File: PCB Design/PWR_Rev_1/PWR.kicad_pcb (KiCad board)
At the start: 2 copper layers, 40 x 65 mm, 57 parts, among them J1 Conn_01x24_Pin, J2 Conn_01x24_Pin, U1 LMR33630ADDA, U2 LMR33630ADDA, U3 LMR33630ADDA

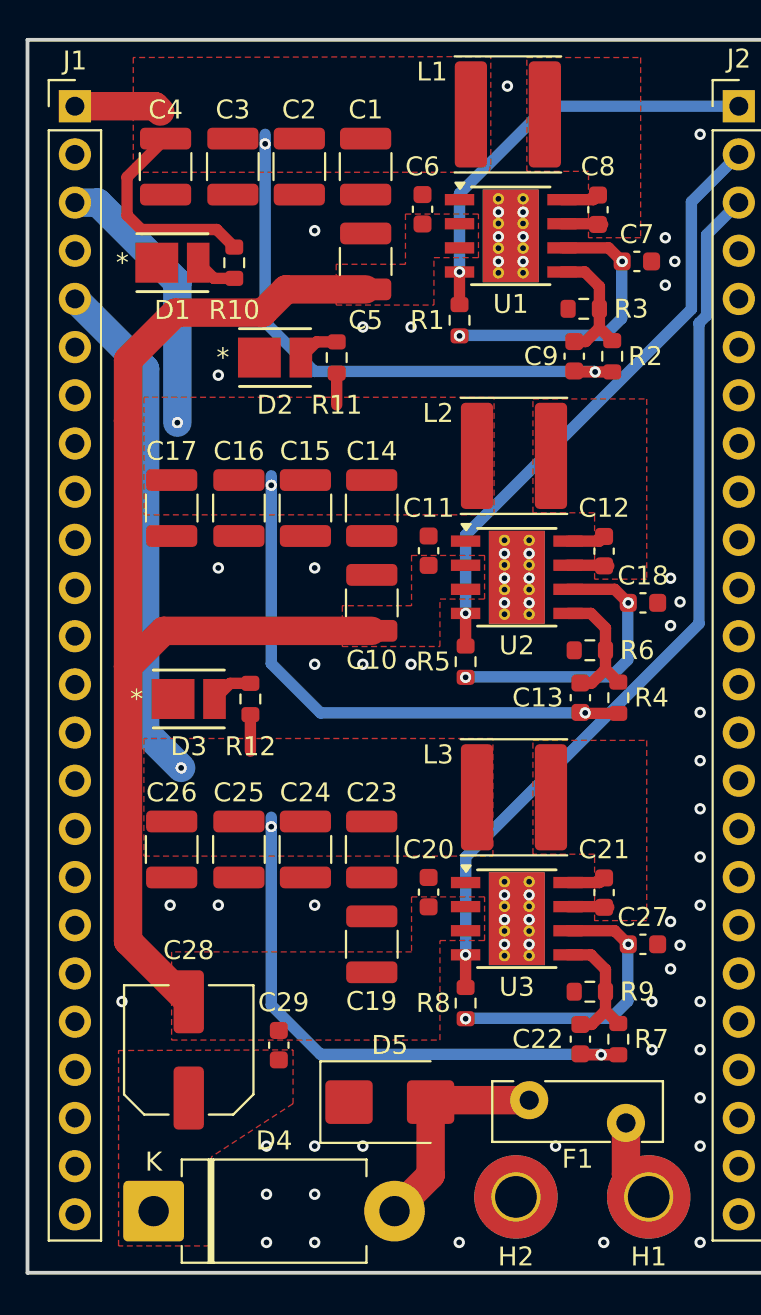
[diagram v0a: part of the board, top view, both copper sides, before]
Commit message: Fixed Schematic Errors
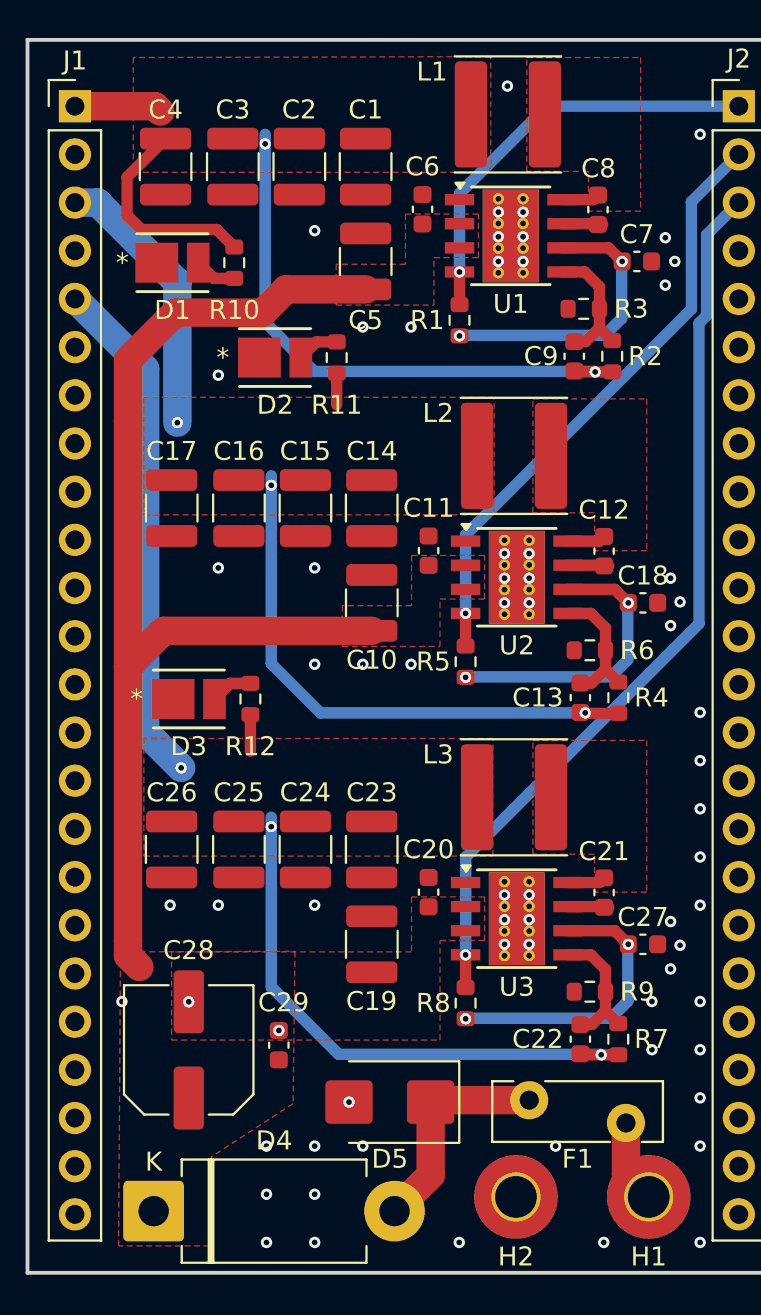
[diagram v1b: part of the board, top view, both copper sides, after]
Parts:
- R7: value 100k -> N/A
- R9: value 9.09k -> N/A
- turned C12 to -90 degrees
- turned C21 to -90 degrees
- turned C8 to -90 degrees
- turned D5 to 180 degrees
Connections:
- C12 pad 1: Net-(U2-BOOT) -> Net-(U2-SW)
- C12 pad 2: Net-(U2-SW) -> Net-(U2-BOOT)
- C21 pad 1: Net-(U3-BOOT) -> Net-(U3-SW)
- C21 pad 2: Net-(U3-SW) -> Net-(U3-BOOT)
- C28 pad 1: Net-(D4-K) -> VIN
- C28 pad 2: VIN -> GND
- C29 pad 1: Net-(D4-K) -> VIN
- C29 pad 2: VIN -> GND
- C8 pad 1: Net-(U1-BOOT) -> Net-(U1-SW)
- C8 pad 2: Net-(U1-SW) -> Net-(U1-BOOT)
- D4 pad 1: Net-(D4-K) -> VIN
- D5 pad 1: GND -> Net-(D4-A)
- D5 pad 2: Net-(D4-A) -> GND
- L1 pad 1: Net-(U1-BOOT) -> Net-(U1-SW)
- L2 pad 1: Net-(U2-BOOT) -> Net-(U2-SW)
- L3 pad 1: Net-(U3-BOOT) -> Net-(U3-SW)
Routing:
- net VIN: track 62.9 -> 60.0 mm
- net V_Piezo: track 59.4 -> 58.8 mm
- net GND: vias 64 -> 67
- added copper zone on F.Cu, net Net-(U1-SW)
- added copper zone on F.Cu, net Net-(U2-SW)
- added copper zone on F.Cu, net Net-(U3-SW)
- removed copper zone on F.Cu, net Net-(D4-K)
- removed copper zone on F.Cu, net Net-(U1-BOOT)
- removed copper zone on F.Cu, net Net-(U2-BOOT)
- removed copper zone on F.Cu, net Net-(U3-BOOT)
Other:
- board text added: "POWER BOARD REV1.1 03/2026 By Samantha Chong"
- board text removed: "POWER BOARD REV1 03/2026 By Samantha Chong"

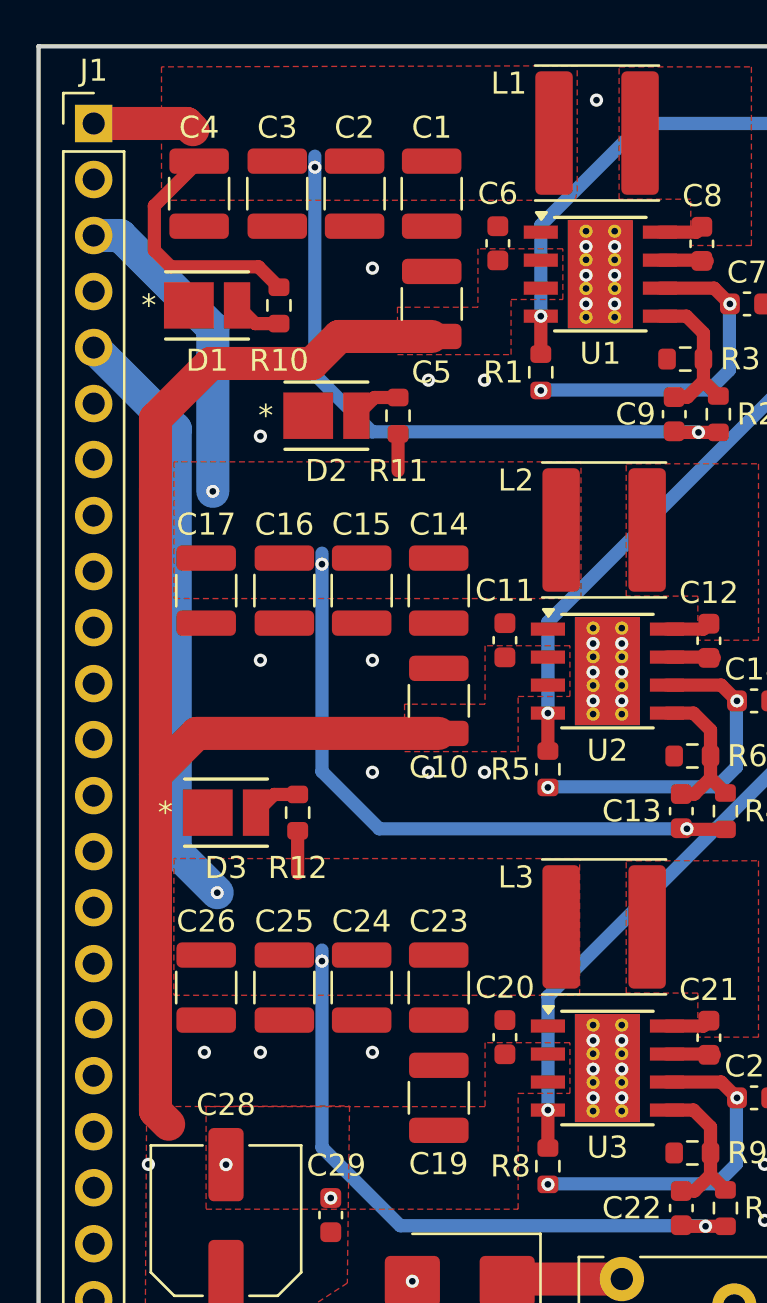
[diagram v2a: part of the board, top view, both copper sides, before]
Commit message: PWR - Updated 3D Models for Full Board Export
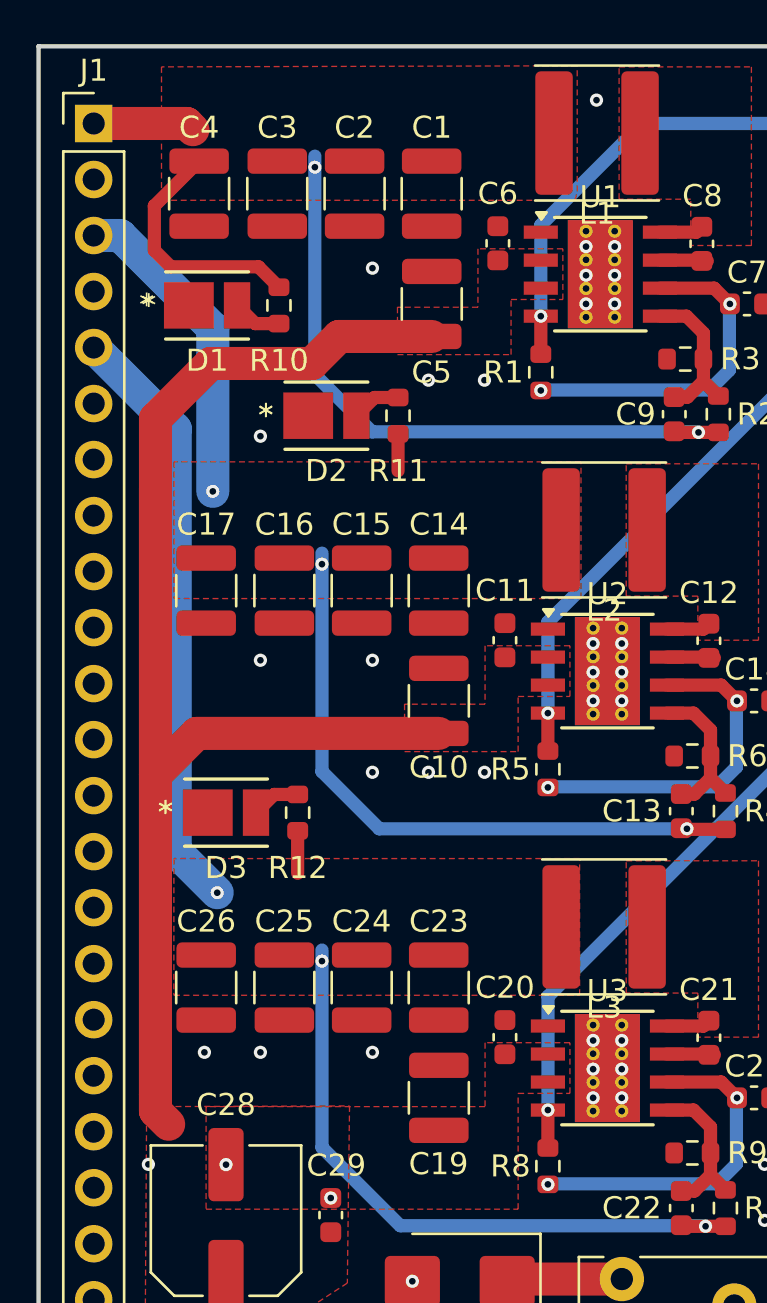
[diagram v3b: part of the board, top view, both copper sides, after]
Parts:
- F1: footprint Fuse:Fuse_Bourns_MF-RHT300 -> PWR_Library:Fuse_Bourns_MF-RHT300
- L1, L2: footprint Inductor_SMD:L_Wuerth_MAPI-5030 -> PWR_Library:L_Wuerth_MAPI-5030
- L3: value 15u -> N/A; footprint Inductor_SMD:L_Wuerth_MAPI-5030 -> PWR_Library:L_Wuerth_MAPI-5030
- U1, U2, U3: footprint Package_SO:Texas_HSOP-8-1EP_3.9x4.9mm_P1.27mm_ThermalVias -> PWR_Library:Texas_HSOP-8-1EP_3.9x4.9mm_P1.27mm_ThermalVias
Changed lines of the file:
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@@
 		)
 	)
-	(footprint "Fuse:Fuse_Bourns_MF-RHT300"
+	(footprint "PWR_Library:Fuse_Bourns_MF-RHT300"
 		(layer "F.Cu")
 		(at 165.44869 125.6175 180)
@@
 		(tags "ptc resettable fuse polyfuse THT")
 		(property "Reference" "F1"
-			(at 2.55 -1.9 0)
+			(at 2.55 -1.9 180)
 			(layer "F.SilkS")
 			(effects
@@
 		)
 		(property "Value" "MF-R300"
-			(at 2.55 3.1 0)
+			(at 2.55 3.1 180)
 			(layer "F.Fab")
 			(effects
@@
 		)
 		(property "Datasheet" "~"
-			(at 0 0 0)
+			(at 0 0 180)
 			(layer "F.Fab")
 			(hide yes)
@@
 		)
 		(property "Description" "Resettable fuse, polymeric positive temperature coefficient"
-			(at 0 0 0)
+			(at 0 0 180)
 			(layer "F.Fab")
 			(hide yes)
@@
 		)
 		(fp_text user "${REFERENCE}"
-			(at 2.55 0.6 0)
+			(at 2.55 0.6 180)
 			(layer "F.Fab")
 			(effects
@@
 		)
 		(embedded_fonts no)
-		(model "${KICAD9_3DMODEL_DIR}/Fuse.3dshapes/Fuse_Bourns_MF-RHT300.step"
+		(model "${KIPRJMOD}/PWR_Library.pretty/MF-R300.stp"
 			(offset
-				(xyz 0 0 0)
+				(xyz -3.5 0 15)
 			)
 			(scale
@@
 			)
 			(rotate
-				(xyz 0 0 0)
+				(xyz -90 -0 -0)
 			)
 		)
@@
 		)
 	)
-	(footprint "Package_SO:Texas_HSOP-8-1EP_3.9x4.9mm_P1.27mm_ThermalVias"
+	(footprint "PWR_Library:Texas_HSOP-8-1EP_3.9x4.9mm_P1.27mm_ThermalVias"
 		(layer "F.Cu")
 		(at 159.695 96.85)
@@
 		(tags "HSOP 1.27")
 		(property "Reference" "U2"
-			(at 0 3.6 0)
+			(at 0 -3.5 0)
 			(layer "F.SilkS")
 			(effects
@@
 		)
 		(embedded_fonts no)
-		(model "${KICAD9_3DMODEL_DIR}/Package_SO.3dshapes/HTSOP-8-1EP_3.9x4.9mm_Pitch1.27mm.step"
+		(model "${KIPRJMOD}/PWR_Library.pretty/DDA0008B.stp"
 			(offset
 				(xyz 0 0 0)
@@
 		)
 	)
-	(footprint "Inductor_SMD:L_Wuerth_MAPI-5030"
+	(footprint "PWR_Library:L_Wuerth_MAPI-5030"
 		(layer "F.Cu")
 		(at 159.545 90.45 180)
@@
 		(tags "Würth -SMT")
 		(property "Reference" "L2"
-			(at 4 2.249999 0)
+			(at 0 -3.65 180)
 			(layer "F.SilkS")
 			(effects
@@
 		)
 		(property "Value" "15u"
-			(at 0 3.65 0)
+			(at 0 3.65 180)
 			(layer "F.Fab")
 			(effects
@@
 		)
 		(property "Datasheet" "~"
-			(at 0 0 0)
+			(at 0 0 180)
 			(layer "F.Fab")
 			(hide yes)
@@
 		)
 		(property "Description" "Inductor"
-			(at 0 0 0)
+			(at 0 0 180)
 			(layer "F.Fab")
 			(hide yes)
@@
 		)
 		(fp_text user "${REFERENCE}"
-			(at 0 0 0)
+			(at 0 0 180)
 			(layer "F.Fab")
 			(effects
@@
 		)
 		(embedded_fonts no)
-		(model "${KICAD9_3DMODEL_DIR}/Inductor_SMD.3dshapes/L_Wuerth_MAPI-5030.step"
+		(model "${KIPRJMOD}/PWR_Library.pretty/STP_WE-MXGI_5030+%28rev1%29.stp"
 			(offset
 				(xyz 0 0 0)
@@
 		)
 	)
-	(footprint "Package_SO:Texas_HSOP-8-1EP_3.9x4.9mm_P1.27mm_ThermalVias"
+	(footprint "PWR_Library:Texas_HSOP-8-1EP_3.9x4.9mm_P1.27mm_ThermalVias"
 		(layer "F.Cu")
 		(at 159.37369 78.85)
@@
 		(tags "HSOP 1.27")
 		(property "Reference" "U1"
-			(at 0 3.6 0)
+			(at 0 -3.5 0)
 			(layer "F.SilkS")
 			(effects
@@
 		)
 		(embedded_fonts no)
-		(model "${KICAD9_3DMODEL_DIR}/Package_SO.3dshapes/HTSOP-8-1EP_3.9x4.9mm_Pitch1.27mm.step"
+		(model "${KIPRJMOD}/PWR_Library.pretty/DDA0008B.stp"
 			(offset
 				(xyz 0 0 0)
@@
 		)
 		(fp_text user "*"
+			(at -2.74 -0.03 0)
+			(unlocked yes)
+			(layer "F.SilkS")
+			(effects
+				(font
+					(size 1 1)
+					(thickness 0.15)
+				)
+			)
+		)
+		(fp_text user "*"
 			(at -2.75 0 0)
 			(unlocked yes)
@@
 		)
 		(embedded_fonts no)
+		(model "${KIPRJMOD}/PWR_Library.pretty/LED_JE2835_CRW/LED_JE2835_CRW.step"
+			(offset
+				(xyz 0 0 0)
+			)
+			(scale
+				(xyz 1 1 1)
+			)
+			(rotate
+				(xyz -0 -0 -0)
+			)
+		)
 	)
 	(footprint "PWR_Library:LED_JE2835_CRW"
@@
 			)
 		)
+		(fp_text user "*"
+			(at -2.74 -0.03 0)
+			(unlocked yes)
+			(layer "F.SilkS")
+			(effects
+				(font
+					(size 1 1)
+					(thickness 0.15)
+				)
+			)
+		)
 		(fp_text user "${REFERENCE}"
 			(at 0 0 0)
@@
 		)
 		(embedded_fonts no)
+		(model "${KIPRJMOD}/PWR_Library.pretty/LED_JE2835_CRW/LED_JE2835_CRW.step"
+			(offset
+				(xyz 0 0 0)
+			)
+			(scale
+				(xyz 1 1 1)
+			)
+			(rotate
+				(xyz -0 -0 -0)
+			)
+		)
 	)
-	(footprint "Package_SO:Texas_HSOP-8-1EP_3.9x4.9mm_P1.27mm_ThermalVias"
+	(footprint "PWR_Library:Texas_HSOP-8-1EP_3.9x4.9mm_P1.27mm_ThermalVias"
 		(layer "F.Cu")
 		(at 159.695 114.85)
@@
 		(tags "HSOP 1.27")
 		(property "Reference" "U3"
-			(at 0 3.6 0)
+			(at 0 -3.5 0)
 			(layer "F.SilkS")
 			(effects
@@
 		)
 		(embedded_fonts no)
-		(model "${KICAD9_3DMODEL_DIR}/Package_SO.3dshapes/HTSOP-8-1EP_3.9x4.9mm_Pitch1.27mm.step"
+		(model "${KIPRJMOD}/PWR_Library.pretty/DDA0008B.stp"
 			(offset
 				(xyz 0 0 0)
@@
 		)
 		(fp_text user "*"
+			(at -2.74 -0.03 0)
+			(unlocked yes)
+			(layer "F.SilkS")
+			(effects
+				(font
+					(size 1 1)
+					(thickness 0.15)
+				)
+			)
+		)
+		(fp_text user "*"
 			(at -2.75 0 0)
 			(unlocked yes)
@@
 		)
 		(embedded_fonts no)
+		(model "${KIPRJMOD}/PWR_Library.pretty/LED_JE2835_CRW/LED_JE2835_CRW.step"
+			(offset
+				(xyz 0 0 0)
+			)
+			(scale
+				(xyz 1 1 1)
+			)
+			(rotate
+				(xyz -0 -0 -0)
+			)
+		)
 	)
 	(footprint "Capacitor_SMD:C_1210_3225Metric"
@@
 		)
 	)
-	(footprint "Inductor_SMD:L_Wuerth_MAPI-5030"
+	(footprint "PWR_Library:L_Wuerth_MAPI-5030"
 		(layer "F.Cu")
 		(at 159.545 108.45 180)
@@
 		(tags "Würth -SMT")
 		(property "Reference" "L3"
-			(at 4 2.249999 0)
+			(at 0 -3.65 180)
 			(layer "F.SilkS")
 			(effects
@@
 			)
 		)
-		(property "Value" "15u"
-			(at 0 3.65 0)
+		(property "Value" "N/A"
+			(at 0 3.65 180)
 			(layer "F.Fab")
 			(effects
@@
 		)
 		(property "Datasheet" "~"
-			(at 0 0 0)
+			(at 0 0 180)
 			(layer "F.Fab")
 			(hide yes)
@@
 		)
 		(property "Description" "Inductor"
-			(at 0 0 0)
+			(at 0 0 180)
 			(layer "F.Fab")
 			(hide yes)
@@
 		)
 		(fp_text user "${REFERENCE}"
-			(at 0 0 0)
+			(at 0 0 180)
 			(layer "F.Fab")
 			(effects
@@
 		)
 		(embedded_fonts no)
-		(model "${KICAD9_3DMODEL_DIR}/Inductor_SMD.3dshapes/L_Wuerth_MAPI-5030.step"
+		(model "${KIPRJMOD}/PWR_Library.pretty/STP_WE-MXGI_5030+%28rev1%29.stp"
 			(offset
 				(xyz 0 0 0)
@@
 		)
 	)
-	(footprint "Inductor_SMD:L_Wuerth_MAPI-5030"
+	(footprint "PWR_Library:L_Wuerth_MAPI-5030"
 		(layer "F.Cu")
 		(at 159.22369 72.45 180)
@@
 		(tags "Würth -SMT")
 		(property "Reference" "L1"
-			(at 4 2.25 0)
+			(at 0 -3.65 180)
 			(layer "F.SilkS")
 			(effects
@@
 		)
 		(property "Value" "6.8u"
-			(at 0 3.65 0)
+			(at 0 3.65 180)
 			(layer "F.Fab")
 			(effects
@@
 		)
 		(property "Datasheet" "~"
-			(at 0 0 0)
+			(at 0 0 180)
 			(layer "F.Fab")
 			(hide yes)
@@
 		)
 		(property "Description" "Inductor"
-			(at 0 0 0)
+			(at 0 0 180)
 			(layer "F.Fab")
 			(hide yes)
@@
 		)
 		(fp_text user "${REFERENCE}"
-			(at 0 0 0)
+			(at 0 0 180)
 			(layer "F.Fab")
 			(effects
@@
 		)
 		(embedded_fonts no)
-		(model "${KICAD9_3DMODEL_DIR}/Inductor_SMD.3dshapes/L_Wuerth_MAPI-5030.step"
+		(model "${KIPRJMOD}/PWR_Library.pretty/STP_WE-MXGI_5030+%28rev1%29.stp"
 			(offset
 				(xyz 0 0 0)

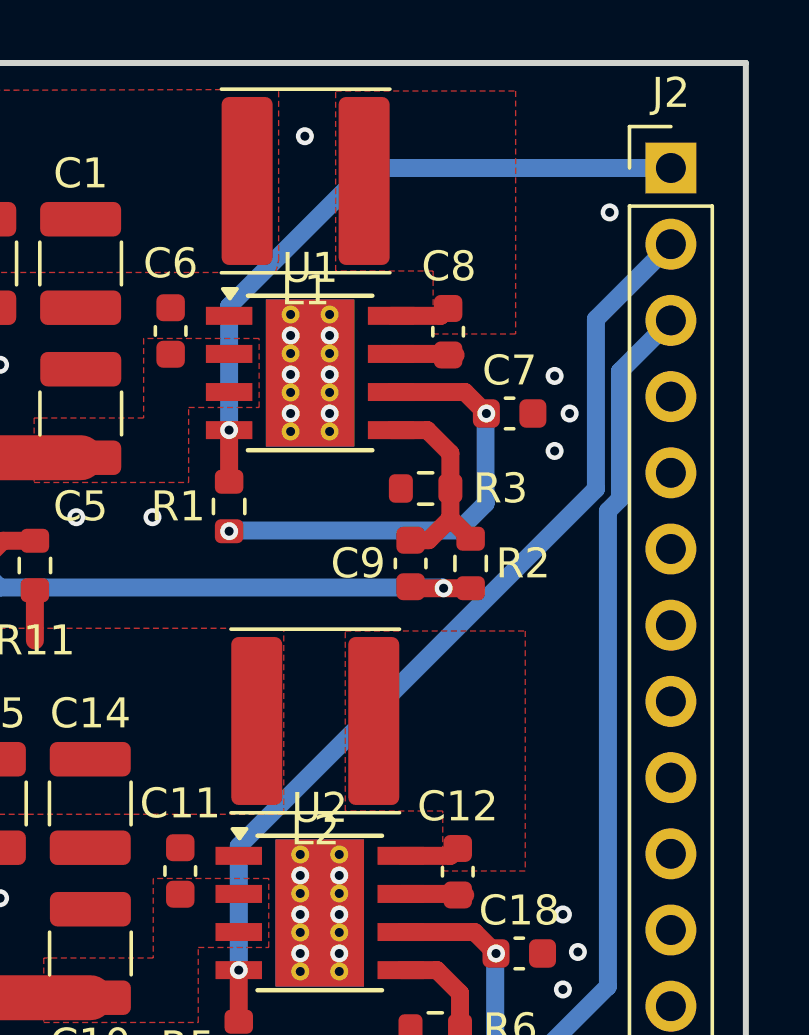
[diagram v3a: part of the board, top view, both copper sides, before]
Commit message: Added Voltage Divider
Added Voltage Divider to 3.3PG and 12VPG
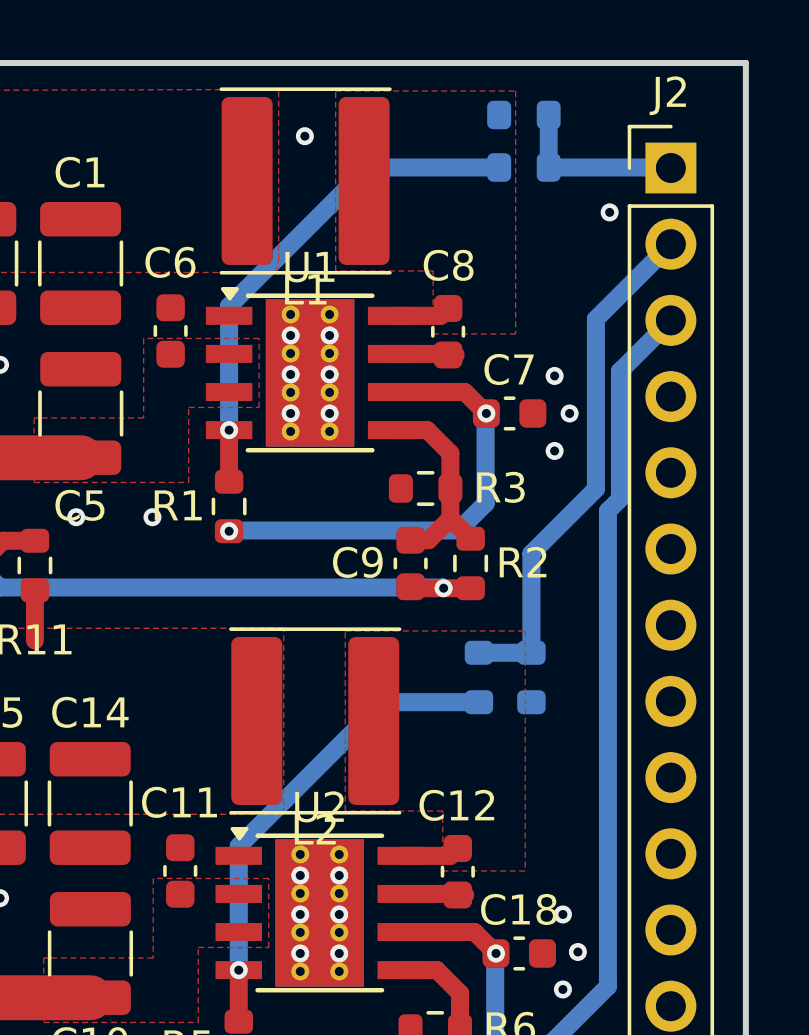
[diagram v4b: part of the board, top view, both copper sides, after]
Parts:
- added R13: 100k, Resistor_SMD:R_0603_1608Metric, B.Cu at (166.5, 72.0)
- added R14: 51k, Resistor_SMD:R_0603_1608Metric, B.Cu at (166.5, 70.2)
- added R15: 100k, Resistor_SMD:R_0603_1608Metric, B.Cu at (165.0, 89.0)
- added R16: 51k, Resistor_SMD:R_0603_1608Metric, B.Cu at (166.8, 89.0)
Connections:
- R1 pad 1: /PG_3.3V -> /PG_3.3V_IC
- R5 pad 1: /PG_12V -> /PG_12V_IC
- R8 pad 1: /PG_VPiezo -> /PG_VPiezo_IC
- U1 pad 4: /PG_3.3V -> /PG_3.3V_IC
- U2 pad 4: /PG_12V -> /PG_12V_IC
- U3 pad 4: /PG_VPiezo -> /PG_VPiezo_IC
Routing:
- net /PG_3.3V_IC: track 0.00 -> 16.8 mm, vias 0 -> 1
- net /PG_3.3V: track 22.5 -> 5.83 mm, vias 1 -> 0
- net /PG_12V_IC: track 0.00 -> 15.8 mm, vias 0 -> 1
- net /PG_12V: track 31.9 -> 17.3 mm, vias 1 -> 0
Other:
- board text added: "POWER BOARD REV1.2 04/2026 By Samantha Chong"
- board text removed: "POWER BOARD REV1.1 03/2026 By Samantha Chong"
